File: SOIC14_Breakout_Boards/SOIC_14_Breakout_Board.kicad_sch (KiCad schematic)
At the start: 6 parts, among them J1 Conn_01x07, J2 Conn_01x07, J3 Conn_01x01, J4 Conn_01x01

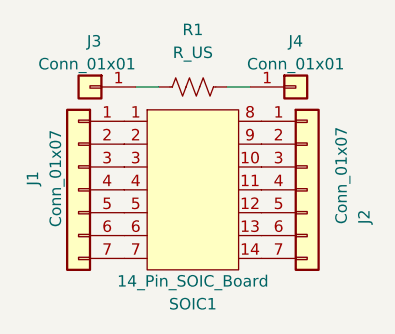
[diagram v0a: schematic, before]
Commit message: Created PCB designs for the 14, 16 & 20 pic SOIC's
Finalized and committed pcb designs for the 14, 16, and 20 SOIC breakout boards
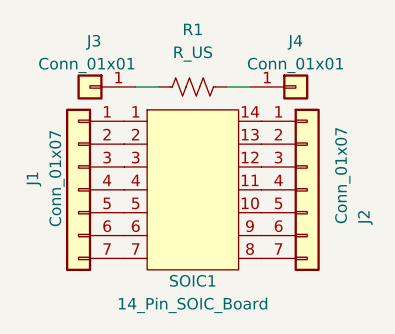
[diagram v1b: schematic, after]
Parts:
- J1, J2: footprint (none) -> Connector_PinSocket_2.54mm:PinSocket_1x07_P2.54mm_Vertical
- SOIC1: footprint (none) -> SOIC_Footprints:14_Pin_SOIC_Board
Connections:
- net at SOIC1.10: now also J2.5 (Pin_5); no longer J2.3 (Pin_3)
- net at SOIC1.12: now also J2.3 (Pin_3); no longer J2.5 (Pin_5)
- net at SOIC1.13: now also J2.2 (Pin_2); no longer J2.6 (Pin_6)
- net at SOIC1.14: now also J2.1 (Pin_1); no longer J2.7 (Pin_7)
- net at SOIC1.8: now also J2.7 (Pin_7); no longer J2.1 (Pin_1)
- net at SOIC1.9: now also J2.6 (Pin_6); no longer J2.2 (Pin_2)
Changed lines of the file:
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@@
     (pin "1")
-  )
-  (symbol (lib_id "Connector_Generic:Conn_01x07") (at 142.24 74.93 0) (mirror y) (unit 1)
-    (in_bom yes) (on_board yes)
-    (property "Reference" "J1" (id 0) (at 137.16 73.66 90))
-    (property "Value" "Conn_01x07" (id 1) (at 139.7 73.66 90))
-    (property "Footprint" "" (id 2) (at 142.24 74.93 0)
-      (effects (font (size 1.27 1.27)) hide)
-    )
-    (property "Datasheet" "~" (id 3) (at 142.24 74.93 0)
-      (effects (font (size 1.27 1.27)) hide)
-    )
-    (pin "1")
-    (pin "2")
-    (pin "3")
-    (pin "4")
-    (pin "5")
-    (pin "6")
-    (pin "7")
   )
   (symbol (lib_id "8_Pin_SOIC_Board:14_Pin_SOIC_Board") (at 154.94 71.12 0) (unit 1)
     (in_bom yes) (on_board yes)
-    (property "Reference" "SOIC1" (id 0) (at 154.94 87.63 0))
-    (property "Value" "14_Pin_SOIC_Board" (id 1) (at 154.94 85.09 0))
-    (property "Footprint" "" (id 2) (at 153.67 74.93 0)
+    (property "Reference" "SOIC1" (id 0) (at 154.94 85.09 0))
+    (property "Value" "14_Pin_SOIC_Board" (id 1) (at 154.94 87.63 0))
+    (property "Footprint" "SOIC_Footprints:14_Pin_SOIC_Board" (id 2) (at 153.67 74.93 0)
       (effects (font (size 1.27 1.27)) hide)
     )
@@
     (pin "8")
     (pin "9")
+  )
+  (symbol (lib_id "Connector_Generic:Conn_01x07") (at 142.24 74.93 0) (mirror y) (unit 1)
+    (in_bom yes) (on_board yes)
+    (property "Reference" "J1" (id 0) (at 137.16 73.66 90))
+    (property "Value" "Conn_01x07" (id 1) (at 139.7 73.66 90))
+    (property "Footprint" "Connector_PinSocket_2.54mm:PinSocket_1x07_P2.54mm_Vertical" (id 2) (at 142.24 74.93 0)
+      (effects (font (size 1.27 1.27)) hide)
+    )
+    (property "Datasheet" "~" (id 3) (at 142.24 74.93 0)
+      (effects (font (size 1.27 1.27)) hide)
+    )
+    (pin "1")
+    (pin "2")
+    (pin "3")
+    (pin "4")
+    (pin "5")
+    (pin "6")
+    (pin "7")
   )
   (symbol (lib_id "Connector_Generic:Conn_01x01") (at 143.51 63.5 0) (mirror y) (unit 1)
@@
       (effects (font (size 1.27 1.27)) (justify left))
     )
-    (property "Footprint" "" (id 2) (at 167.64 74.93 0)
+    (property "Footprint" "Connector_PinSocket_2.54mm:PinSocket_1x07_P2.54mm_Vertical" (id 2) (at 167.64 74.93 0)
       (effects (font (size 1.27 1.27)) hide)
     )
@@
   (symbol_instances
     (path "/62ccd677-3164-4152-aa0f-6cb86f838284"
-      (reference "J1") (unit 1) (value "Conn_01x07") (footprint "")
+      (reference "J1") (unit 1) (value "Conn_01x07") (footprint "Connector_PinSocket_2.54mm:PinSocket_1x07_P2.54mm_Vertical")
     )
     (path "/d20a2b1b-f2f9-4a5b-a3dc-832dd74372a3"
-      (reference "J2") (unit 1) (value "Conn_01x07") (footprint "")
+      (reference "J2") (unit 1) (value "Conn_01x07") (footprint "Connector_PinSocket_2.54mm:PinSocket_1x07_P2.54mm_Vertical")
     )
     (path "/7dfc8e4d-cb13-4be6-bcf8-32029bab029b"
@@
       (reference "R1") (unit 1) (value "R_US") (footprint "Resistor_SMD:R_0805_2012Metric")
     )
-    (path "/765e172b-1b5a-4c83-a5c3-0126938b8fb3"
-      (reference "SOIC1") (unit 1) (value "14_Pin_SOIC_Board") (footprint "")
+    (path "/3d4e0053-ac73-4b5d-adfe-b11e70eaaf85"
+      (reference "SOIC1") (unit 1) (value "14_Pin_SOIC_Board") (footprint "SOIC_Footprints:14_Pin_SOIC_Board")
     )
   )
